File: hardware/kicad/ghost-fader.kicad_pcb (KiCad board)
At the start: 2 copper layers, 108 x 80 mm, 74 parts, among them J1 NRJ6HF, J2 NRJ6HF, J3 NRJ6HF, J4 NRJ6HF, SW1 MIDI channel, U1 THAT1246S08, U2 THAT1246S08, U3 PGA2310PA, U4 PGA2310PA, U5 OPA2134PA, U6 THAT1646S08, U7 THAT1646S08, U9 Teensy 4.0

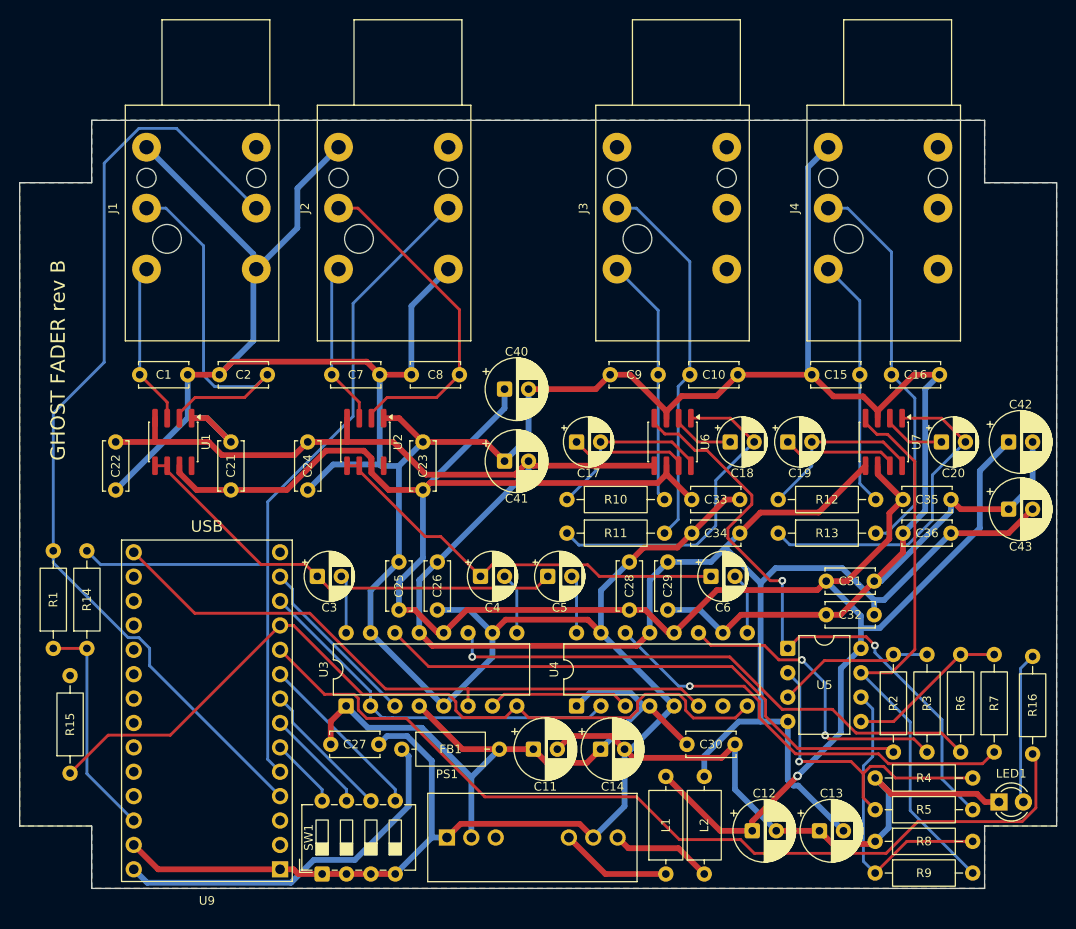
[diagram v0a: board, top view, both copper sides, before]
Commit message: Label every part on the silkscreen
Reference designators now sit beside each part instead of under it:
a per-part label table in build_pcb.py plus rules per footprint type
(vertical discs and axials labelled beside/above, radial cans above or
below). The summer block on the right was opened up so the resistor
rows have room for labels; L2 and the R4/R5/R8/R9 rows shifted a
little, C12/C13 moved up beside U5, R16 back to the left column.
Re-routed, DRC still 0 errors; gerbers and site renders regenerated.

Co-Authored-By: Claude Fable 5.1 <noreply@anthropic.com>
Claude-Session: https://claude.ai/code/session_015P372fhz9Ee8MTRWGXMeho
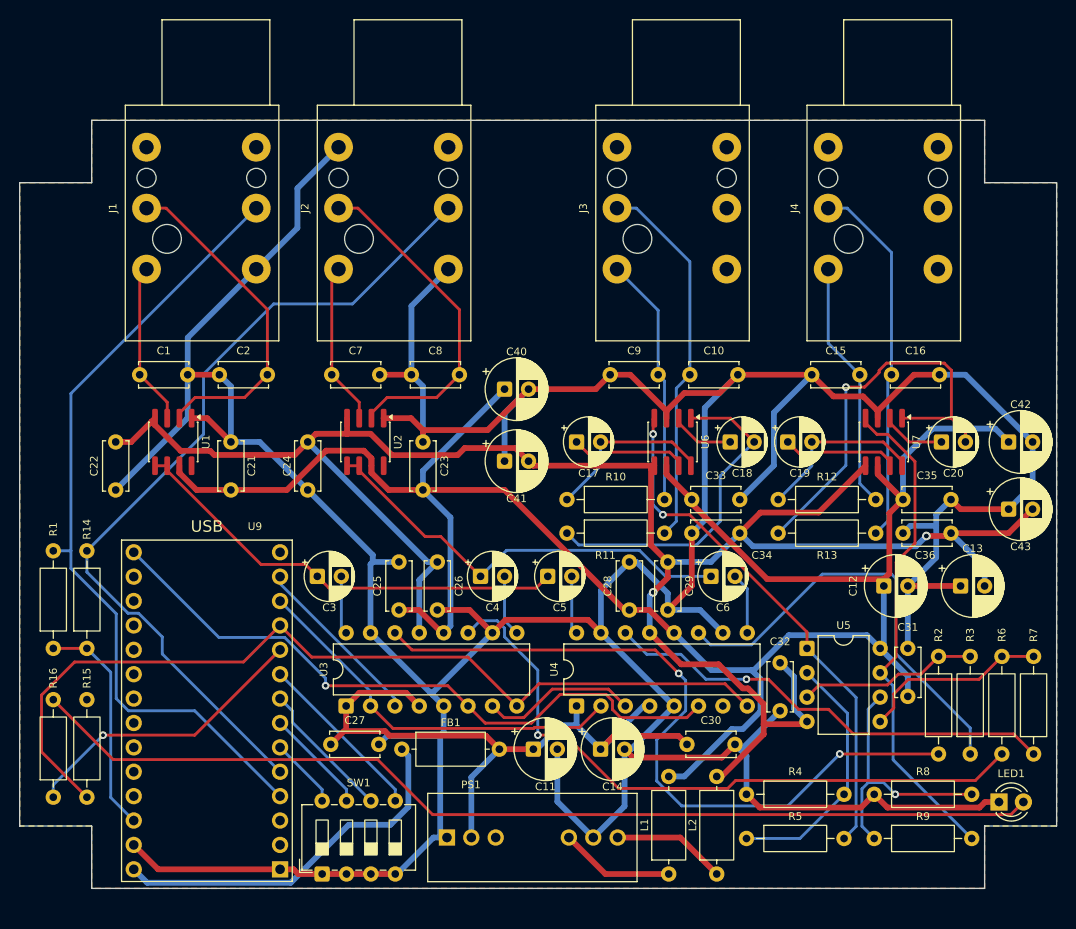
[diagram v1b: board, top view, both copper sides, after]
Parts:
- moved R16 102.1 mm to (3.50, 70.5)
- moved C13 29.4 mm to (98.0, 48.5)
- moved C12 28.9 mm to (90.0, 48.5)
- moved C31 14.7 mm to (92.5, 60.0), turned to 90 degrees
- moved R5 13.7 mm to (75.7, 74.8)
- moved R4 13.5 mm to (75.7, 70.2)
- moved C32 11.1 mm to (79.2, 61.5), turned to 90 degrees
- moved R8 4.90 mm to (89.0, 70.2)
- moved R2 4.70 mm to (95.7, 66.0)
- moved R3 4.50 mm to (99.0, 66.0)
- moved R6 4.30 mm to (102.3, 66.0)
- moved R7 4.10 mm to (105.6, 66.0)
- moved R9 3.60 mm to (89.0, 74.8)
- moved R15 3.05 mm to (7.00, 70.5)
- moved U5 2.00 mm to (82.0, 55.0)
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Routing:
- net Net-(LED1-A): track 15.8 -> 106.5 mm
- net LED: track 95.9 -> 30.7 mm, vias 0 -> 1
- net GND: track 547.5 -> 499.5 mm
- net Net-(U3-VOUTL): track 58.0 -> 76.7 mm, vias 0 -> 2
- net -15V: track 226.8 -> 210.4 mm, vias 0 -> 2
- net SENSE_L: track 99.3 -> 84.1 mm
- net Net-(U4-VOUTR): track 32.1 -> 45.8 mm, vias 2 -> 0
- net +15V: track 227.2 -> 214.3 mm, vias 1 -> 0
- net Net-(U3-VOUTR): track 57.7 -> 69.3 mm
- net L_OUT_SE: track 65.4 -> 54.8 mm
- net Net-(U7-Out-): track 34.8 -> 43.8 mm, vias 0 -> 1
- net ~{MUTE}: track 86.1 -> 94.5 mm
- net R_OUT_SE: track 59.2 -> 52.0 mm
- net Net-(U5A--): track 33.5 -> 26.6 mm, vias 1 -> 0
- net Net-(U1-In-): track 40.1 -> 35.1 mm
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
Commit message: Rev C: XIAO RP2040 and Traco TBA 2-0522 replace the Teensy 4.0 and TMR 3
Tier 1 cost-down, no change to the audio path. U9 becomes a Seeed XIAO
RP2040 on header pins (USB-C, TinyUSB MIDI, its 5V pin is VBUS straight
through), PS1 becomes a 2 W unregulated Traco TBA 2-0522 on KiCad's stock
SIP-7 footprint. Rails are now +/-12 V: the +/-15 V TBA 2-0523 would pass
the PGA2310's 16 V absolute maximum at light load. Parts cost drops from
about $145 to about $110.

- gen.py: TBA2_Dual and XIAO_RP2040 symbols, XIAO footprint (Seeed pin
  numbering, USB-C overhang drawn), control sheet rewired to D0-D10,
  power sheet and notes for the unregulated converter, +/-12V rails.
- check.py: new U9 / PS1 pins; NETLIST OK. ERC 0/0.
- Both boards rebuilt and re-routed (Freerouting 1.9), DRC 0 errors; the
  only warnings are jack-nose and USB-C shell silk over the board edge.
- Gerbers, drill, zips, BOM, schematic SVG/PDF and board renders
  regenerated. README and site updated: pin map, power budget
  (~250 mA typical), level budget at +/-12 V, parts list and totals.

Co-Authored-By: Claude Fable 5.1 <noreply@anthropic.com>
Claude-Session: https://claude.ai/code/session_01C8uqpe49go1TPWMsWKKVkn
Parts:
- PS1: value TMR 3-0523 -> TBA 2-0522; footprint GhostFader:TRACO_TMR3_SIP8 -> Converter_DCDC:Converter_DCDC_TRACO_TBA2-xxxx_Dual_THT
- U9: value Teensy 4.0 -> XIAO RP2040; footprint GhostFader:Teensy40_Edge -> GhostFader:XIAO_RP2040_THT
- moved U9 6.60 mm to (19.5, 68.1)
- moved PS1 1.70 mm to (44.5, 73.0), turned to 90 degrees
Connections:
- net +15V renamed +12V
- net -15V renamed -12V
- PS1 pad 1: GND -> +5V
- PS1 pad 2: +5V -> GND
- SW1 pad 5: Net-(U9-7) -> Net-(U9-D5/SCL/GP7)
- SW1 pad 6: Net-(U9-6) -> Net-(U9-D4/SDA/GP6)
- SW1 pad 7: Net-(U9-5) -> Net-(U9-D3/GP29)
- SW1 pad 8: Net-(U9-4) -> Net-(U9-D2/GP28)
- U9 pad 1: GND -> SENSE_L
- U9 pad 11: ~{MUTE} -> SDI
- U9 pad 12: ~{CS} -> +3V3
- U9 pad 13: SDI -> GND
- U9 pad 14: unconnected-(U9-12-Pad14) -> USB_5V
- U9 pad 2: unconnected-(U9-0-Pad2) -> SENSE_R
- U9 pad 3: unconnected-(U9-1-Pad3) -> Net-(U9-D2/GP28)
- U9 pad 4: SENSE_L -> Net-(U9-D3/GP29)
- U9 pad 5: SENSE_R -> Net-(U9-D4/SDA/GP6)
- U9 pad 6: Net-(U9-4) -> Net-(U9-D5/SCL/GP7)
- U9 pad 7: Net-(U9-5) -> ~{MUTE}
- U9 pad 8: Net-(U9-6) -> ~{CS}
- U9 pad 9: Net-(U9-7) -> SCLK
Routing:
- net Net-(U3-VOUTR): track 69.3 -> 93.9 mm, vias 1 -> 3
- net LED: track 30.7 -> 10.4 mm, vias 1 -> 0
- net Net-(U9-7): track 18.2 -> 0.00 mm
- net /2x2 gain matrix and summers/L_SUM: track 18.8 -> 36.0 mm
- net R_OUT_SE: track 52.0 -> 69.2 mm
- net Net-(U9-D5/SCL/GP7): track 0.00 -> 16.8 mm
- net Net-(LED1-A): track 106.5 -> 122.0 mm
- net Net-(U3-VOUTL): track 76.7 -> 61.8 mm, vias 2 -> 0
- net Net-(U9-6): track 14.6 -> 0.00 mm
- net SDI: track 18.4 -> 33.0 mm, vias 0 -> 1
- net Net-(U4-VOUTL): track 47.7 -> 61.9 mm
- net Net-(U4-VOUTR): track 45.8 -> 33.5 mm
- net Net-(PS1--Vout): track 11.9 -> 23.9 mm
- net ~{CS}: track 40.8 -> 52.5 mm
- net Net-(U9-D4/SDA/GP6): track 0.00 -> 11.7 mm
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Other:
- board text added: "GHOST FADER rev C"
- board text removed: "GHOST FADER rev B"

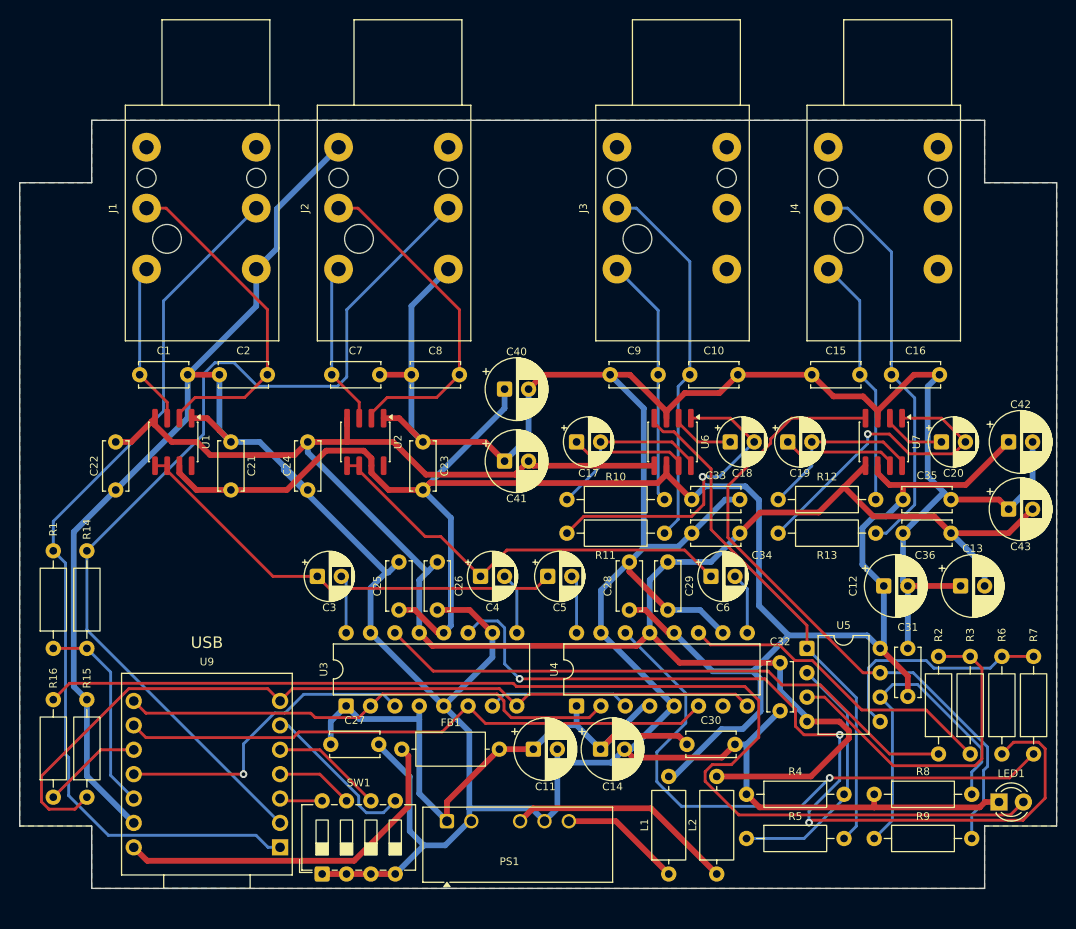
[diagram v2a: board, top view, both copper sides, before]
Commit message: Rev D: isolate the audio ground from USB
Add a TI ISO7762FDW digital isolator on the four control lines and two
plug-sense lines, a 78L05 that makes +5VA from +12 V for the PGA logic
and the isolator's audio side, and a split ground: GND_USB (XIAO, USB-C,
switch, LED, ferrite, reservoir, DC-DC input) and GND (everything audio).
The two meet only through C45 (1 nF) and R17 (1 M) at PS1. The sense
pull-ups drop from 1 M to 100 k for the isolator's input leakage.

Both boards get two ground pours per layer with a 2 mm copper-free gap
and a rule area that keeps the router out; U8 and PS1 straddle the gap.
The 1590BB board's island is the front-left corner; the narrow board's
is a pocket under the XIAO with the audio ground wrapping beneath it.
ERC 0, netlist checked (61 nets, 263 pins), DRC clean on both routed
boards, and a script check confirms no copper crosses the gap.

README, docs page, schematic exports, renders, gerbers and BOM regenerated.

Co-Authored-By: Claude Fable 5.1 <noreply@anthropic.com>
Claude-Session: https://claude.ai/code/session_013C8baRPktSQjwfdzSRwmAq
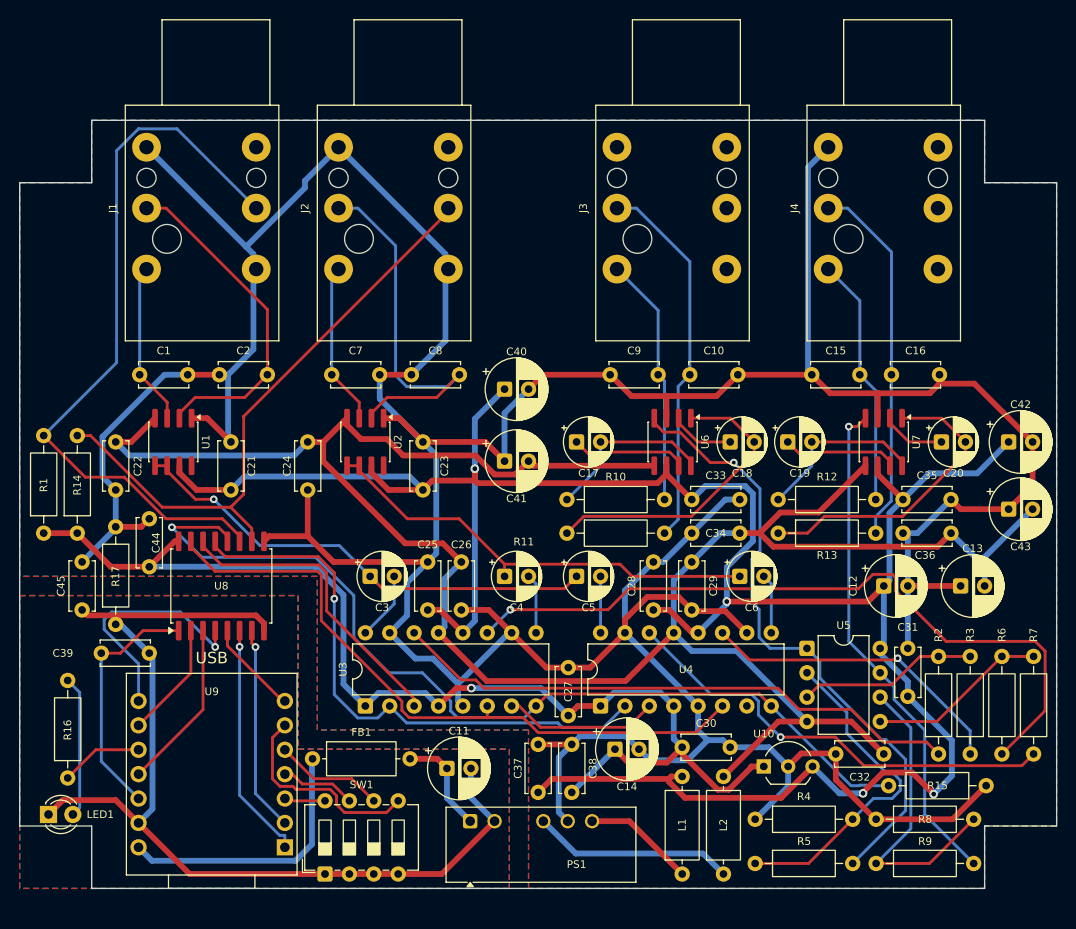
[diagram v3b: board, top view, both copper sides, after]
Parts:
- added C37: 100n, Capacitor_THT:C_Disc_D5.0mm_W2.5mm_P5.00mm, F.Cu at (54.0, 70.0)
- added C38: 100n, Capacitor_THT:C_Disc_D5.0mm_W2.5mm_P5.00mm, F.Cu at (57.5, 70.0)
- added C39: 100n, Capacitor_THT:C_Disc_D5.0mm_W2.5mm_P5.00mm, F.Cu at (8.50, 55.5)
- added C44: 100n, Capacitor_THT:C_Disc_D5.0mm_W2.5mm_P5.00mm, F.Cu at (13.5, 46.5)
- added C45: 1n 1kV, Capacitor_THT:C_Disc_D5.0mm_W2.5mm_P5.00mm, F.Cu at (6.50, 51.0)
- added R17: 1M, Resistor_THT:R_Axial_DIN0207_L6.3mm_D2.5mm_P10.16mm_Horizontal, F.Cu at (10.0, 52.5)
- added U10: L78L05, Package_TO_SOT_THT:TO-92_Inline_Wide, F.Cu at (77.5, 67.3)
- added U8: ISO7762FDW, Package_SO:SOIC-16W_7.5x10.3mm_P1.27mm, F.Cu at (21.0, 48.5)
- R1, R14: value 1M -> 100k
- moved LED1 99.0 mm to (3.00, 72.3)
- moved R15 83.5 mm to (90.5, 69.3), turned to 0 degrees
- moved C27 24.9 mm to (57.1, 62.0), turned to 90 degrees
- moved R1 12.0 mm to (2.50, 43.0)
- moved R14 12.0 mm to (6.00, 43.0)
- moved FB1 9.35 mm to (30.5, 66.5)
- moved C11 9.22 mm to (44.5, 67.5)
- moved C32 7.34 mm to (85.0, 66.0), turned to 0 degrees
- moved C3 5.50 mm to (36.5, 47.5)
- moved C25 3.00 mm to (42.5, 51.0)
- moved C5 3.00 mm to (58.0, 47.5)
- moved C6 3.00 mm to (75.0, 47.5)
- moved R5 2.75 mm to (76.6, 77.4)
- moved R4 2.75 mm to (76.6, 72.8)
- moved R9 2.61 mm to (89.2, 77.4)
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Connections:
- C11 pad 2: GND -> GND_USB
- C14 pad 1: +5V -> +5VA
- C27 pad 1: +5V -> +5VA
- C30 pad 1: +5V -> +5VA
- LED1 pad 1: GND -> GND_USB
- PS1 pad 2: GND -> GND_USB
- R1 pad 1: +3V3 -> +5VA
- R14 pad 1: +3V3 -> +5VA
- SW1 pad 1: GND -> GND_USB
- SW1 pad 2: GND -> GND_USB
- SW1 pad 3: GND -> GND_USB
- SW1 pad 4: GND -> GND_USB
- U3 pad 1: +5V -> +5VA
- U3 pad 4: +5V -> +5VA
- U4 pad 1: +5V -> +5VA
- U4 pad 4: +5V -> +5VA
- U9 pad 1: SENSE_L -> /Control/MCU_SENSE_L
- U9 pad 11: SDI -> /Control/MCU_SDI
- U9 pad 13: GND -> GND_USB
- U9 pad 2: SENSE_R -> /Control/MCU_SENSE_R
- U9 pad 7: ~{MUTE} -> /Control/MCU_~{MUTE}
- U9 pad 8: ~{CS} -> /Control/MCU_~{CS}
- U9 pad 9: SCLK -> /Control/MCU_SCLK
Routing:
- net +5VA: track 0.00 -> 118.4 mm, vias 0 -> 1
- net Net-(LED1-A): track 122.0 -> 14.8 mm
- net GND_USB: track 0.00 -> 103.4 mm
- net +5V: track 67.3 -> 10.8 mm
- net +12V: track 212.7 -> 247.9 mm, vias 0 -> 4
- net SENSE_R: track 98.9 -> 64.1 mm
- net /Control/MCU_~{CS}: track 0.00 -> 25.1 mm, vias 0 -> 1
- net /Control/MCU_SENSE_L: track 0.00 -> 24.8 mm, vias 0 -> 1
- net /Control/MCU_SENSE_R: track 0.00 -> 21.5 mm, vias 0 -> 1
- net SENSE_L: track 94.9 -> 77.0 mm
- net /Control/MCU_SDI: track 0.00 -> 17.7 mm
- net /2x2 gain matrix and summers/L_SUM: track 36.0 -> 18.8 mm
- net Net-(U3-VOUTR): track 93.9 -> 77.3 mm, vias 3 -> 1
- net R_OUT_SE: track 69.2 -> 53.0 mm, vias 0 -> 1
- net Net-(U4-VOUTL): track 61.9 -> 47.1 mm
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- added copper zone on B.Cu, net GND_USB
- added copper zone on F.Cu, net GND_USB
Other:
- board text added: "AUDIO GND"
- board text added: "GHOST FADER rev D"
- board text added: "USB GND"
- board text removed: "GHOST FADER rev C"
